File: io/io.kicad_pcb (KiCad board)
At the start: 4 copper layers, 102.4 x 40.3 mm, 0 parts

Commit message: Updates to io board
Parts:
- added C10: 4.7u, Capacitor_SMD:C_0402_1005Metric, F.Cu at (125.4, 147.9)
- added C11: 100n, Capacitor_SMD:C_0402_1005Metric, F.Cu at (125.4, 149.8)
- added C12: 100n, Capacitor_SMD:C_0402_1005Metric, F.Cu at (125.4, 151.8)
- added C13: 100n, Capacitor_SMD:C_0402_1005Metric, F.Cu at (125.4, 153.8)
- added C14: 100n, Capacitor_SMD:C_0402_1005Metric, F.Cu at (125.4, 155.7)
- added C15: 100n, Capacitor_SMD:C_0402_1005Metric, F.Cu at (125.4, 157.7)
- added C16: 100n, Capacitor_SMD:C_0402_1005Metric, F.Cu at (125.4, 159.7)
- added C17: 100n, Capacitor_SMD:C_0402_1005Metric, F.Cu at (128.3, 147.9)
- added C18: 100n, Capacitor_SMD:C_0402_1005Metric, F.Cu at (128.3, 149.8)
- added C19: 10u, Capacitor_SMD:C_0805_2012Metric, F.Cu at (183.0, 148.4)
- added C2: 100n, Capacitor_SMD:C_0402_1005Metric, F.Cu at (122.5, 147.9)
- added C20: 100n, Capacitor_SMD:C_0402_1005Metric, F.Cu at (128.3, 151.8)
- added C21: 100n, Capacitor_SMD:C_0402_1005Metric, F.Cu at (128.3, 153.8)
- added C3: 15p, Capacitor_SMD:C_0402_1005Metric, F.Cu at (122.5, 149.8)
- added C4: 15p, Capacitor_SMD:C_0402_1005Metric, F.Cu at (122.5, 151.8)
- added C6: 4.7u, RP2350_80QFN_minimal:C_0402_1005Metric_small_pads, F.Cu at (122.5, 153.8)
- added C7: 4.7u, RP2350_80QFN_minimal:C_0402_1005Metric_small_pads, F.Cu at (122.5, 155.7)
- added C8: 100n, Capacitor_SMD:C_0402_1005Metric, F.Cu at (122.5, 157.7)
- added C9: 4.7u, Capacitor_SMD:C_0402_1005Metric, F.Cu at (122.5, 159.7)
- added Card1: TF-15×15, easyeda2kicad:TF-SMD_TF-15-15, F.Cu at (176.6, 97.0)
- added D1: KT-0603R, LED_SMD:LED_0603_1608Metric, F.Cu at (177.6, 152.7)
- added D2: WS2812B, LED_SMD:LED_WS2812B_PLCC4_5.0x5.0mm_P3.2mm, F.Cu at (121.8, 84.5)
- added D3: 1N4148W, Diode_SMD:D_SOD-123F, F.Cu at (170.2, 162.8)
- added J1: ~, RV4028:ModuleHeader_Single, F.Cu at (133.0, 120.5)
- added J2: Conn_01x03, Connector_PinHeader_2.54mm:PinHeader_1x03_P2.54mm_Vertical, F.Cu at (114.0, 83.3)
- added J3: QwST, Connector_JST:JST_SH_SM04B-SRSS-TB_1x04-1MP_P1.00mm_Horizontal, F.Cu at (151.9, 84.9)
- added J4: SM03B-SRSS-TB, Connector_JST:JST_SH_SM03B-SRSS-TB_1x03-1MP_P1.00mm_Horizontal, F.Cu at (168.4, 84.9)
- added J5: QwST, Connector_JST:JST_SH_SM04B-SRSS-TB_1x04-1MP_P1.00mm_Horizontal, F.Cu at (160.6, 84.9)
- added J6: Conn_02x06_Odd_Even, Connector_PinHeader_2.54mm:PinHeader_2x06_P2.54mm_Vertical, F.Cu at (131.1, 85.9)
- added L1: 3.3u, RP2350_80QFN_minimal:L_pol_2016, F.Cu at (177.3, 156.0)
- added R1: 1k, Resistor_SMD:R_0402_1005Metric, F.Cu at (119.6, 147.9)
- added R2: 1k, Resistor_SMD:R_0402_1005Metric, F.Cu at (119.6, 149.9)
- added R3: 33, Resistor_SMD:R_0402_1005Metric, F.Cu at (119.6, 151.8)
- added R4: 1k, Resistor_SMD:R_0402_1005Metric, F.Cu at (119.6, 153.8)
- added R6: 1k, Resistor_SMD:R_0402_1005Metric, F.Cu at (119.6, 155.8)
- added R7: 27, Resistor_SMD:R_0402_1005Metric, F.Cu at (119.6, 157.8)
- added R8: 27, Resistor_SMD:R_0402_1005Metric, F.Cu at (119.6, 159.8)
- added SW1: SW_Push, Button_Switch_SMD:SW_Push_1P1T_NO_Vertical_Wuerth_434133025816, F.Cu at (90.6, 103.4)
- added SW2: SW_Push, Button_Switch_SMD:SW_Push_1P1T_NO_Vertical_Wuerth_434133025816, F.Cu at (90.6, 107.5)
- added U1: RP2350_80QFN, RP2350_80QFN_minimal:RP2350-QFN-80-1EP_10x10_P0.4mm_EP3.4x3.4mm_ThermalVias, F.Cu at (137.3, 100.8)
- added U2: 74AHC32, Package_SO:SOIC-14_3.9x8.7mm_P1.27mm, F.Cu at (105.4, 106.7)
- added U3: W25Q32JVS, Package_SO:SOIC-8_5.3x5.3mm_P1.27mm, F.Cu at (121.4, 93.0)
- added Y1: ABM8-272-T3, Crystal:Crystal_SMD_3225-4Pin_3.2x2.5mm, F.Cu at (178.2, 149.1)

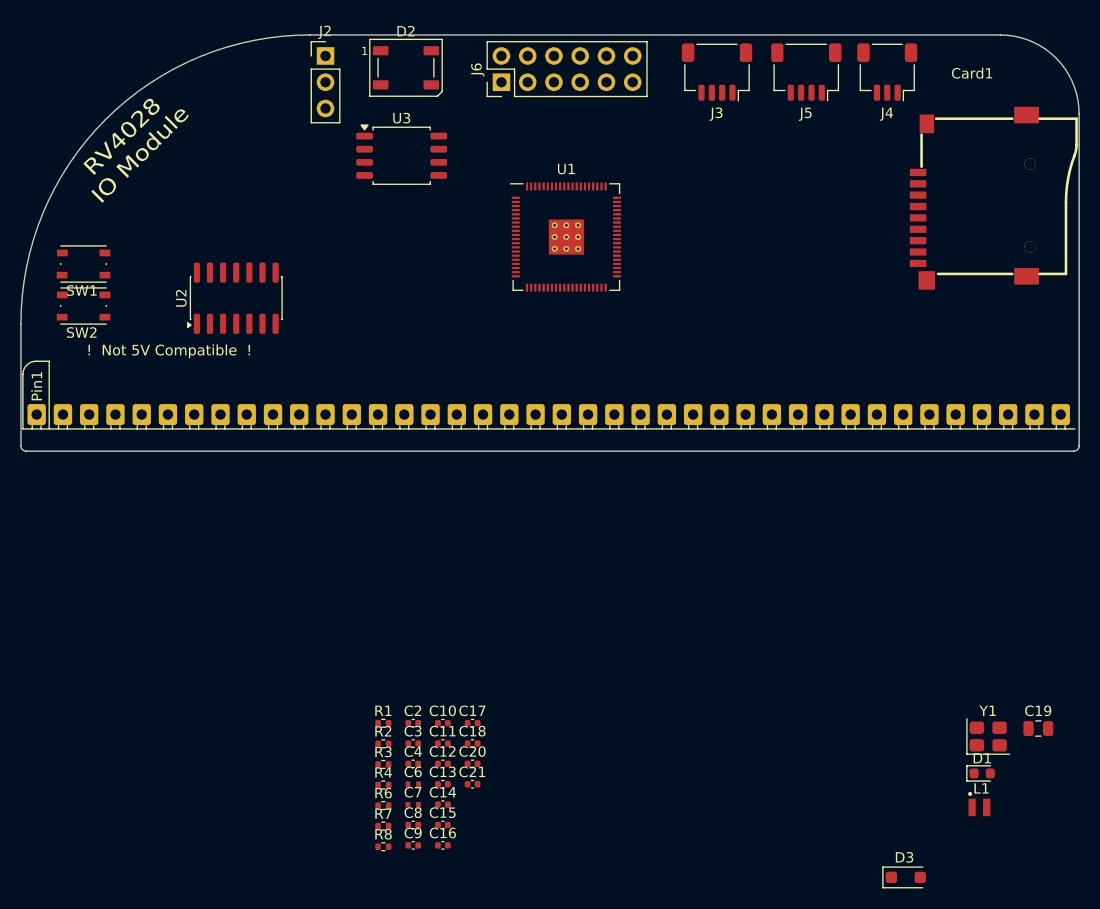
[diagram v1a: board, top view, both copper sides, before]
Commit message: IO module routed
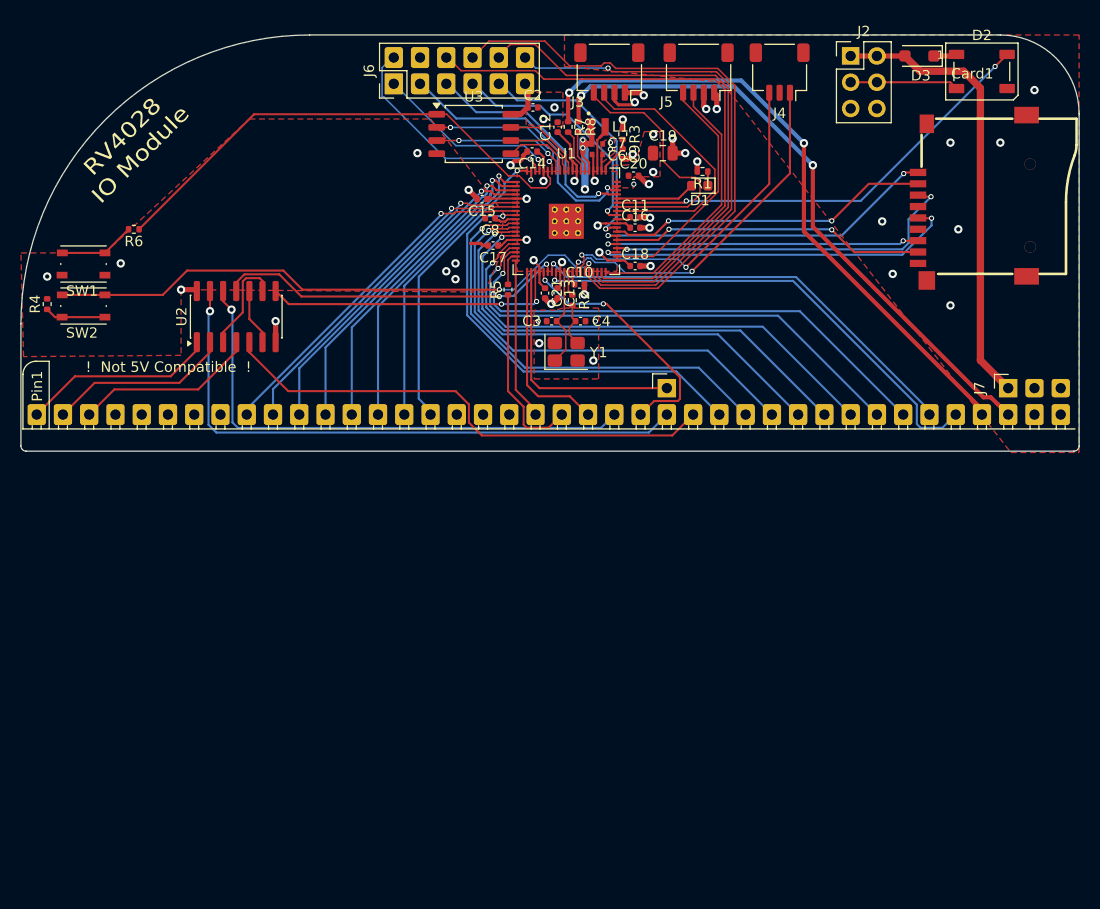
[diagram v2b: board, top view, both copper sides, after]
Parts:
- added J7: Conn_01x03, Connector_PinSocket_2.54mm:PinSocket_1x03_P2.54mm_Vertical, F.Cu at (180.1, 115.4)
- added J8: Conn_01x01, Connector_PinHeader_2.54mm:PinHeader_1x01_P2.54mm_Vertical, F.Cu at (147.1, 115.4)
- added R5: 27, Resistor_SMD:R_0402_1005Metric, F.Cu at (131.7, 105.9)
- J2: value Conn_01x03 -> Conn_02x03; footprint Connector_PinHeader_2.54mm:PinHeader_1x03_P2.54mm_Vertical -> Connector_PinHeader_2.54mm:PinHeader_2x03_P2.54mm_Vertical
- U1: footprint RP2350_80QFN_minimal:RP2350-QFN-80-1EP_10x10_P0.4mm_EP3.4x3.4mm_ThermalVias -> RV4028:RP2350-QFN-80-1EP_10x10_P0.4mm_EP3.4x3.4mm_ThermalVias
- moved D3 79.5 mm to (171.5, 83.3), turned to 180 degrees
- moved L1 75.5 mm to (140.4, 90.2)
- moved R8 72.2 mm to (138.5, 90.2), turned to -90 degrees
- moved R7 70.0 mm to (137.5, 90.2), turned to -90 degrees
- moved C9 69.9 mm to (142.8, 92.8), turned to -90 degrees
- moved C19 66.5 mm to (146.7, 92.7)
- moved C7 66.3 mm to (140.3, 91.8)
- moved R3 65.2 mm to (142.8, 90.9), turned to -90 degrees
- moved C14 63.8 mm to (134.0, 92.6), turned to 180 degrees
- moved C6 63.5 mm to (140.3, 92.8)
- moved D1 63.1 mm to (150.2, 95.9), turned to 180 degrees
- moved C12 62.6 mm to (136.5, 90.2), turned to 90 degrees
- moved C16 62.6 mm to (144.0, 99.9)
- moved R1 61.7 mm to (150.5, 94.5), turned to 180 degrees
- moved R6 60.7 mm to (95.5, 100.1), turned to 180 degrees
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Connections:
- J2 pad 2: /WS2812_DAT -> +5V
- J2 pad 3: GND -> /WS2812_DAT
- U1 pad 19: /CLK -> Net-(U1-GPIO19)
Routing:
- net /USB_D+: track 0.00 -> 61.9 mm, vias 0 -> 2
- net /USB_D-: track 0.00 -> 60.9 mm, vias 0 -> 2
- net /SPI_RX: track 0.00 -> 58.4 mm
- net /~{RD}: track 0.00 -> 58.4 mm, vias 0 -> 1
- net /RUN: track 0.00 -> 55.8 mm, vias 0 -> 2
- net /SPI_TX: track 0.00 -> 54.9 mm
- net /SPI_CLK: track 0.00 -> 52.2 mm
- net /~{REQ}: track 0.00 -> 50.8 mm, vias 0 -> 1
- net /D7: track 0.00 -> 50.2 mm, vias 0 -> 1
- net /SPI_CS: track 0.00 -> 50.2 mm, vias 0 -> 1
- net /~{A31}: track 0.00 -> 49.1 mm
- net /QSPI_SS: track 0.00 -> 48.9 mm
- net /D6: track 0.00 -> 48.7 mm, vias 0 -> 1
- net /D5: track 0.00 -> 47.3 mm, vias 0 -> 1
- net /UART1_RX: track 0.00 -> 47.2 mm, vias 0 -> 1
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- added copper zone on F.Cu, net +1V1
- added copper zone on F.Cu, net +3V3
- added copper zone on In2.Cu, net +3V3
- added copper zone on F.Cu, net GND
- added copper zone on In1.Cu, net GND
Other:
- board text added: "5V"
- board text added: "~{WT}"

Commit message: RAM module, many tweaks
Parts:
- J6: value Conn_02x06_Odd_Even -> Conn_02x08_Odd_Even; footprint Connector_PinHeader_2.54mm:PinHeader_2x06_P2.54mm_Vertical -> Connector_PinHeader_2.54mm:PinHeader_2x08_P2.54mm_Vertical
- SW1, SW2: footprint Button_Switch_SMD:SW_Push_1P1T_NO_Vertical_Wuerth_434133025816 -> RV4028:SW-SMD_HX-TS-1101-C-W
- moved J6 5.08 mm to (115.6, 86.0)
- moved R4 3.11 mm to (86.2, 110.3), turned to -90 degrees
- moved R6 1.86 mm to (96.9, 101.3)
- moved C2 1.71 mm to (132.8, 89.4)
- moved U3 1.68 mm to (126.8, 91.3)
- moved SW2 0.89 mm to (91.1, 108.3), turned to 0 degrees
- moved J2 0.51 mm to (164.3, 83.3)
- moved SW1 0.46 mm to (91.1, 103.4), turned to 0 degrees
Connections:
- J6 pad 1: /UART0_TX -> +3V3
- J6 pad 10: /SPI_CLK -> /SPI_TX
- J6 pad 11: +3V3 -> /SPI_CS2
- J6 pad 12: /SPI_CS -> /SPI_RX
- J6 pad 2: /UART0_RX -> +3V3
- J6 pad 3: /GPIO47_ADC7 -> GND
- J6 pad 5: /GPIO46_ADC6 -> /UART0_TX
- J6 pad 6: /SPI_TX -> /UART0_RX
- J6 pad 7: /SPI_CS2 -> /GPIO47_ADC7
- J6 pad 8: /SPI_RX -> GND
- J6 pad 9: /SPI_CS1 -> /GPIO46_ADC6
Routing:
- net /RUN: track 55.8 -> 50.4 mm
- net +5V: track 44.0 -> 49.3 mm
- net /~{USB_BOOT}: track 7.36 -> 2.90 mm
- net +3V3: track 43.8 -> 47.7 mm
- net Net-(R4-Pad1): track 5.90 -> 2.07 mm
- net GND: track 25.2 -> 28.9 mm, vias 37 -> 41
- net /QSPI_SD1: track 14.4 -> 16.2 mm
- net /QSPI_SD2: track 13.3 -> 15.1 mm
- net /QSPI_SCLK: track 7.11 -> 8.91 mm
- net /QSPI_SD0: track 6.87 -> 8.58 mm
- net /QSPI_SD3: track 8.06 -> 9.49 mm
- net /QSPI_SS: track 48.9 -> 48.3 mm
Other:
- board text added: "3V3 3V3"
- board text added: "BOOT"
- board text added: "CS 3V3"
- board text added: "DAT"
- board text added: "GND"
- board text added: "GND 47"
- board text added: "GND GND"
- board text added: "I2C0"
- board text added: "I2C1"
- board text added: "RESET"
- board text added: "RX TX"
- board text added: "SCK CS1"
- board text added: "SI CS2"
- board text added: "SO 46"
- board text added: "SWD"
- board text added: "UART SPI"
- board text added: "WS2812"

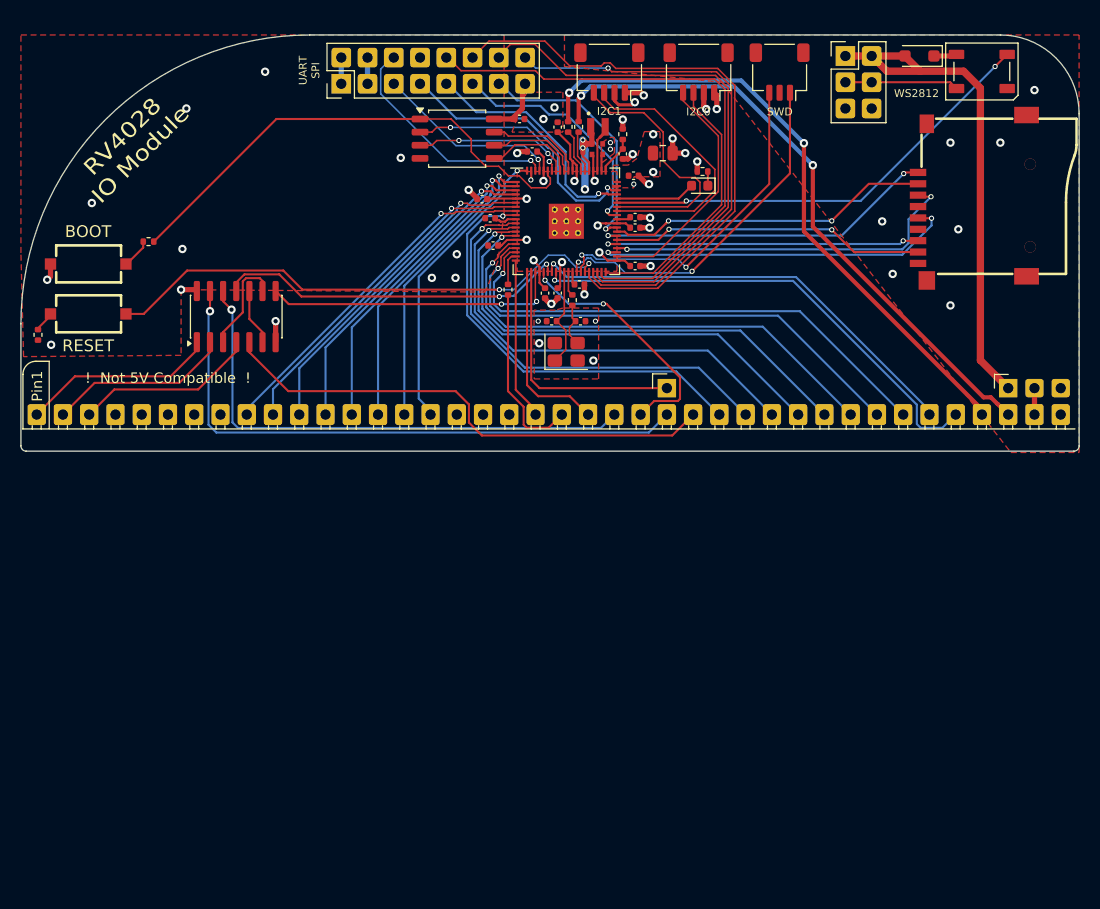
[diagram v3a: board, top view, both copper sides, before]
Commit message: IO module 2mm headers
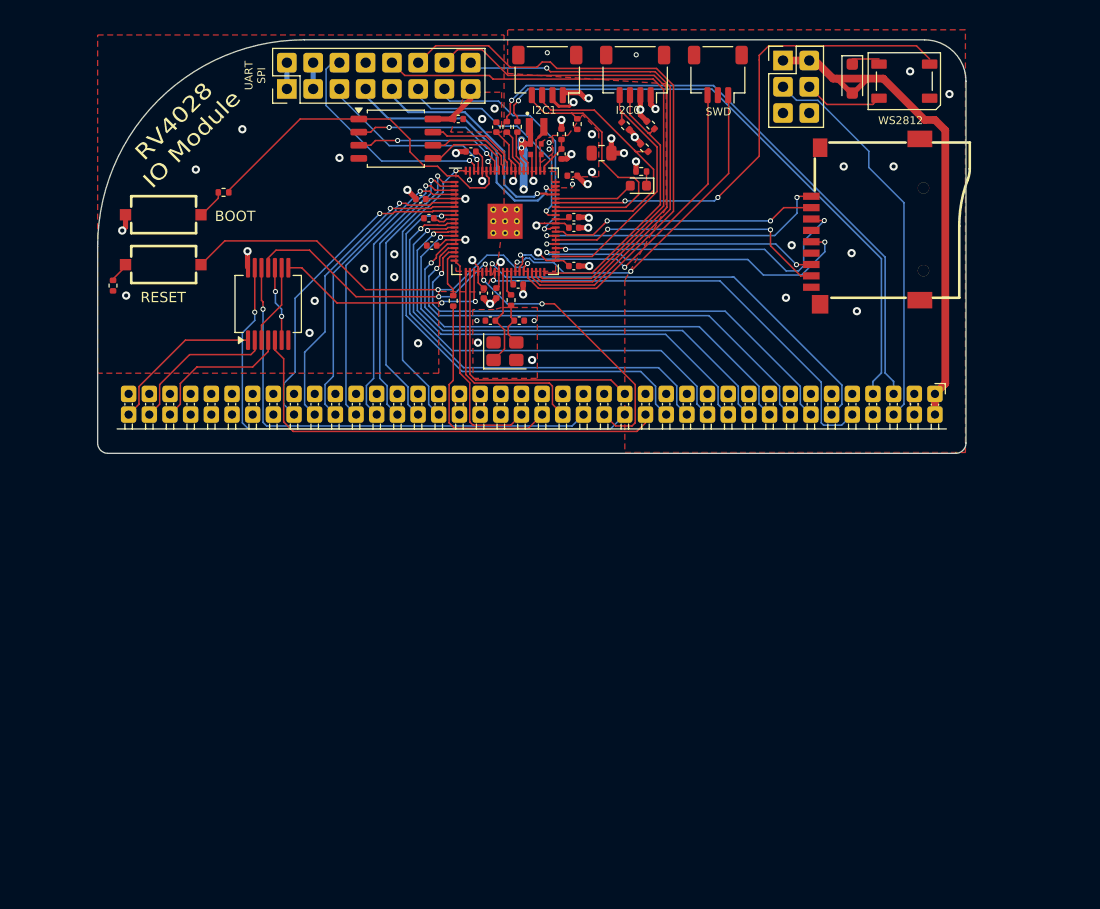
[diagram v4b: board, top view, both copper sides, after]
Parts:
- removed J7: Conn_01x03, Connector_PinSocket_2.54mm:PinSocket_1x03_P2.54mm_Vertical
- removed J8: Conn_01x01, Connector_PinHeader_2.54mm:PinHeader_1x01_P2.54mm_Vertical
- added R10: 10k, Resistor_SMD:R_0402_1005Metric, F.Cu at (143.1, 90.1)
- added R11: 10k, Resistor_SMD:R_0402_1005Metric, F.Cu at (138.4, 89.9)
- added R12: 10k, Resistor_SMD:R_0402_1005Metric, F.Cu at (144.9, 92.2)
- added R9: 10k, Resistor_SMD:R_0402_1005Metric, F.Cu at (145.5, 90.0)
- J1: footprint RV4028:ModuleHeader_Single -> RV4028:Module_2mm
- U2: value 74AHC32 -> 74LVC32; footprint Package_SO:SOIC-14_3.9x8.7mm_P1.27mm -> Package_SO:SSOP-14_5.3x6.2mm_P0.65mm
- moved Card1 10.6 mm to (166.3, 99.3)
- moved R6 8.68 mm to (104.2, 96.5)
- moved SW2 8.68 mm to (98.3, 103.5)
- moved R4 8.68 mm to (93.5, 105.5)
- moved SW1 8.68 mm to (98.3, 98.7)
- moved D2 7.56 mm to (170.0, 85.8)
- moved D3 6.86 mm to (165.0, 85.5), turned to -90 degrees
- moved J5 6.14 mm to (144.0, 85.1)
- moved J2 6.05 mm to (158.3, 83.8)
- moved J3 6.01 mm to (135.5, 85.1)
- moved J4 5.98 mm to (152.0, 85.1)
- moved C6 5.94 mm to (134.4, 92.8)
- moved C7 5.94 mm to (134.4, 91.8)
- moved C3 5.93 mm to (130.0, 108.9)
- moved Y1 5.93 mm to (131.4, 111.9)
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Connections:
- J1 pad 18: unconnected-(J1-PWR-Pad18) -> +3V3
- J1 pad 37: /USB_D+ -> unconnected-(J1-SPARE1-Pad37)
- J1 pad 38: /USB_D- -> /S2
- J1 pad 40: +3V3 -> +5V
- J2 pad 3: /WS2812_DAT -> /S2
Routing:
- net /S2: track 0.00 -> 38.2 mm
- net /QSPI_SS: track 48.3 -> 33.2 mm
- net /RUN: track 50.4 -> 37.6 mm
- net /~{RDREQ}: track 34.2 -> 26.2 mm
- net /~{IOSEL}: track 28.8 -> 22.5 mm
- net /~{RESET}: track 15.7 -> 21.8 mm
- net /SD_D3: track 31.3 -> 25.9 mm
- net /~{RD}: track 58.4 -> 53.3 mm
- net /GPIO44_ADC4: track 43.7 -> 48.7 mm
- net /SD_D2: track 33.4 -> 28.9 mm
- net /~{A31}: track 49.1 -> 44.8 mm
- net /~{REQ}: track 50.8 -> 46.6 mm
- net GND: track 28.9 -> 25.0 mm, vias 41 -> 44
- net /~{INT}: track 18.0 -> 21.9 mm
- net /SD_D0: track 31.0 -> 27.3 mm
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- added copper zone on B.Cu, net +3V3
- added copper zone on In1.Cu, net +3V3
- added copper zone on B.Cu, net GND
- added copper zone on In2.Cu, net GND
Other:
- board size 102.4 x 40.3 mm -> 84 x 40 mm
- board text added: "RV2048 CPU v0.1 © Mike Bell 2026 JLCJLCJLCJLC"
- board text added: "S2"
- board text added: "~{BRQ}"
- board text removed: "! Not 5V Compatible !"
- board text removed: "~{WT}"
